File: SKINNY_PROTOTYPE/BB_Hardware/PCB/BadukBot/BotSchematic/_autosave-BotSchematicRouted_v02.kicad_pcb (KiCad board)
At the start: 4 copper layers, 93 x 44.5 mm, 82 parts, among them J1 MOLEX_78171-0002, J10 A3-16DA-2SV(71), J11 62401621722, J12 A3-16DA-2SV(71), J13 0877601616, J2 MOLEX_78171-0003, M1 Pos-1a, M2 Neg-1a, M3 Pos-2a, M4 Neg-2a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

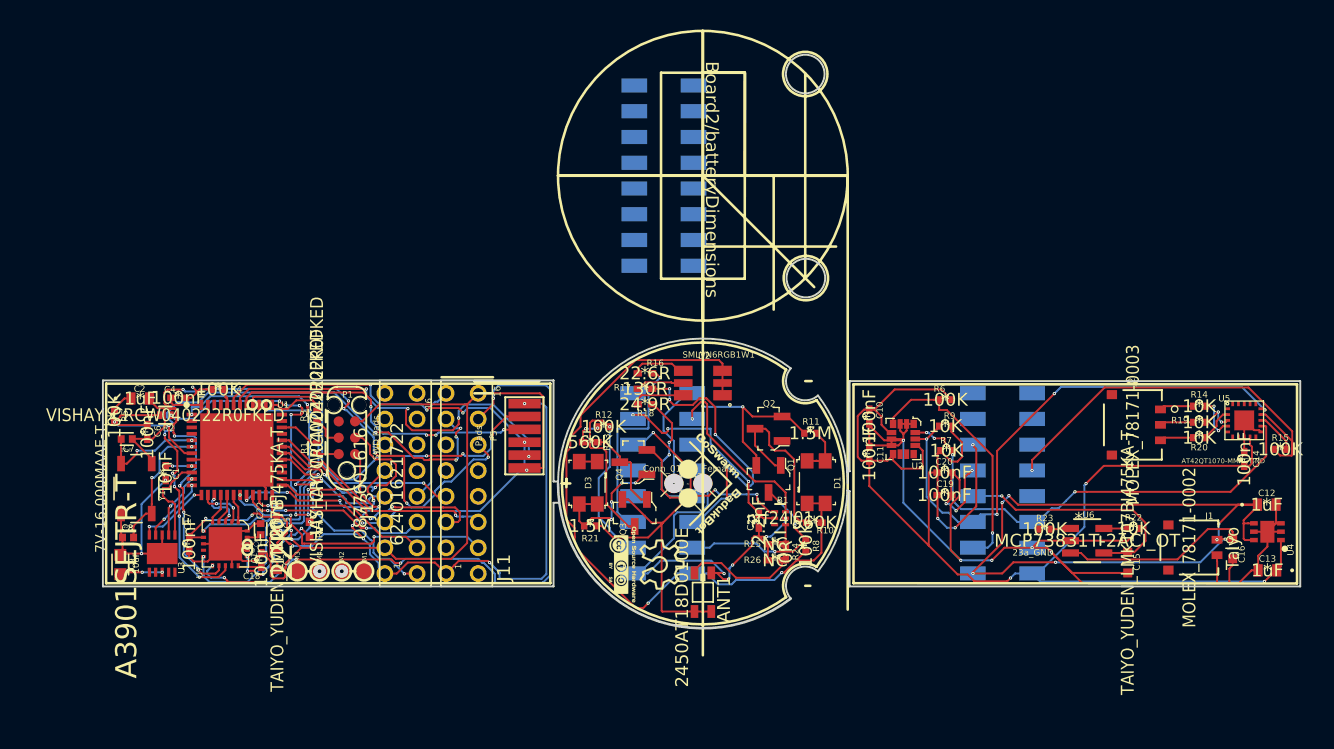
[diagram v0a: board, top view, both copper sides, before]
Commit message: Routed PCBs pending optimization
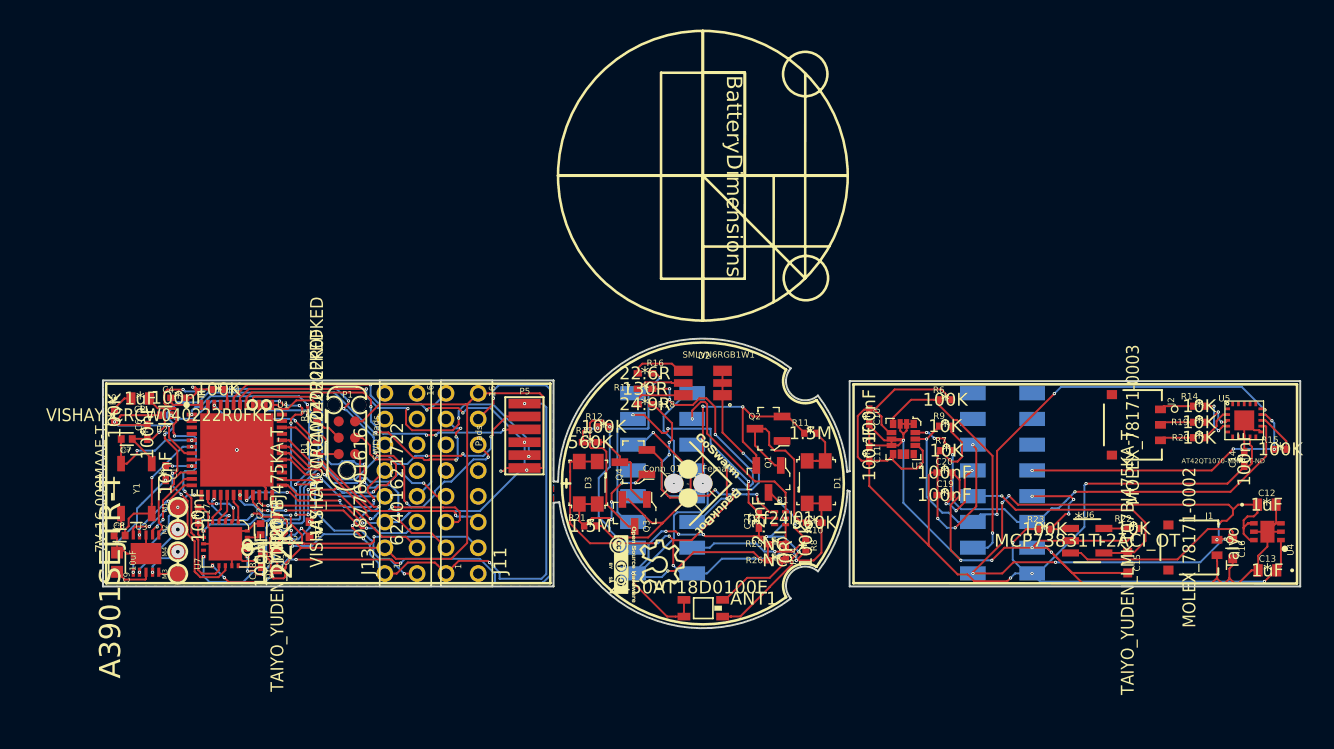
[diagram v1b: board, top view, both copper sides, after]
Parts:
- removed the J12 at (113.9, 83.9)
- J10, J12: footprint A13:A13 -> A13:A13_1
- moved M1 15.3 mm to (75.5, 109.6), turned to 180 degrees
- moved M2 13.1 mm to (75.5, 111.3), turned to 180 degrees
- moved M4 11.1 mm to (75.5, 113.1), turned to 180 degrees
- moved M3 9.29 mm to (75.5, 114.8), turned to 180 degrees
- moved C17 2.32 mm to (77.1, 110.2), turned to 270 degrees
- moved U3 1.25 mm to (73.0, 113.2)
- moved ANT1 1.24 mm to (116.3, 117.5), turned to 180 degrees
- moved C8 0.67 mm to (71.0, 111.8)
- moved C9 0.31 mm to (70.8, 113.9)
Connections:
- J12 pad 10: 23a_Ground -> Net-(J12-Pad10)
- J12 pad 12: 21a_3.3v -> Net-(J12-Pad12)
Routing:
- net 2a_GND: track 12.4 -> 98.3 mm, vias 5 -> 12
- net 15a_GND2: track 69.6 -> 0.00 mm, vias 4 -> 0
- net 3b_PHOTODIODE1: track 0.00 -> 26.6 mm, vias 0 -> 6
- net ~29a_TOUCH_CHG~: track 32.6 -> 22.9 mm, vias 1 -> 4
- net 27a_CHARGING: track 1.56 -> 8.08 mm, vias 0 -> 3
- net Net-(M1-Pad1): track 0.00 -> 6.48 mm, vias 0 -> 2
- net 21a_3.3v: track 115.9 -> 121.3 mm, vias 6 -> 8
- net Net-(M2-Pad1): track 0.00 -> 4.55 mm, vias 1 -> 2
- net 2b_GND: track 115.1 -> 118.8 mm, vias 9 -> 13
- net Net-(M4-Pad1): track 0.00 -> 2.89 mm, vias 1 -> 2
- net Net-(ANT1-Pad1): track 8.85 -> 6.47 mm
- net 10b_SDA: track 51.9 -> 53.7 mm
- net Net-(M3-Pad1): track 0.00 -> 1.53 mm
- net 1a_3.3v: track 59.9 -> 58.4 mm, vias 4 -> 8
- net 1b_3.3v: track 75.7 -> 74.4 mm, vias 13 -> 11
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- added copper zone on F.Cu, net 1b_3.3v
- added copper zone on B.Cu, net 2b_GND
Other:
- board size 93 x 44.5 mm -> 93 x 22.5 mm
- copper layers 4 -> 2
- board text added: "BatteryDimensions"
- board text added: "j13-10"
- board text added: "j13-12"
- board text removed: "10"
- board text removed: "12"
- board text removed: "23a_GND"
- board text removed: "Board2/batteryDimensions"

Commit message: Updates to the BOM; PCB changes
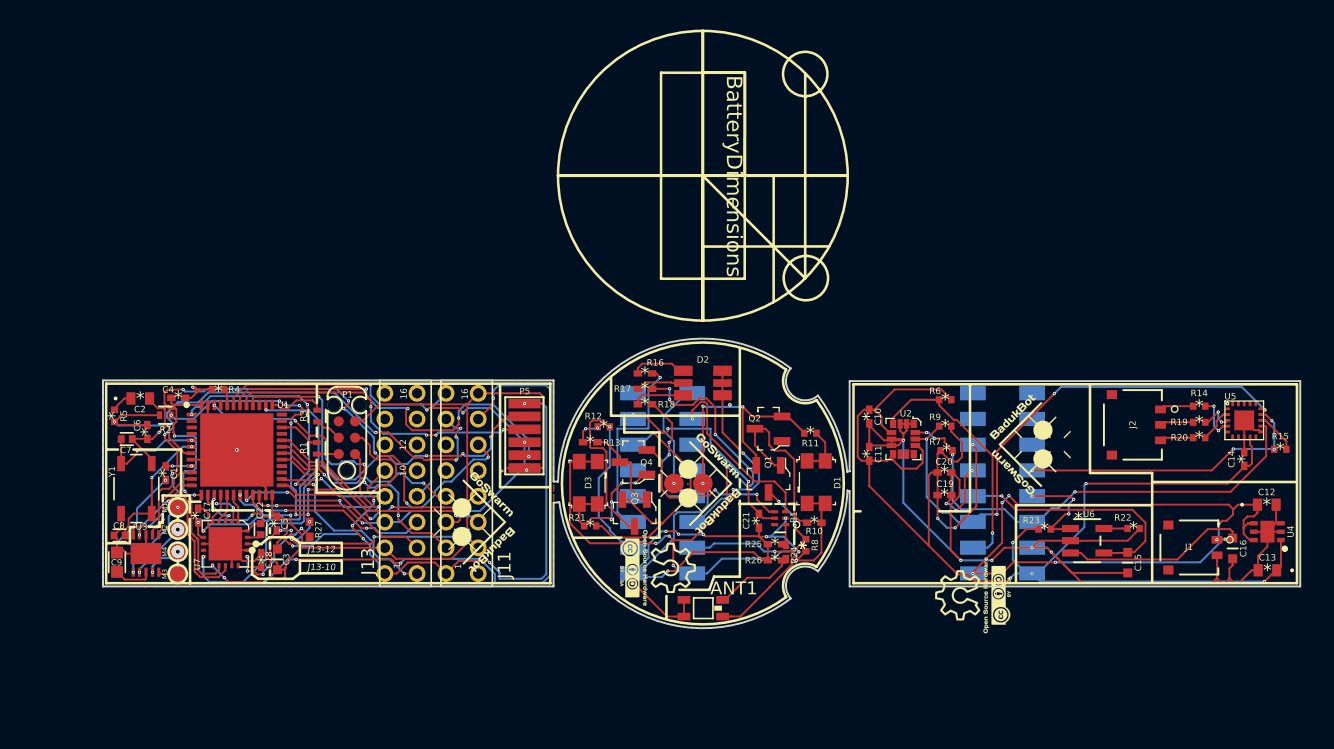
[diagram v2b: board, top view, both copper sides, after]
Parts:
- added G1: LOGO, Silk:BadukBot-GoSwarm, F.Cu at (141.8, 104.8)
- added G1: LOGO, Silk:BadukBot-GoSwarm, F.Cu at (98.5, 110.8)
- added G2: LOGO, Silk:OpenHardwareLogo, F.Cu at (137.2, 116.5)
- added G2: LOGO, Silk:OpenHardwareLogo, B.Cu at (94.2, 107.8)
- moved G2 0.91 mm to (112.8, 114.3)
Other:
- board text added: "10"
- board text added: "12"
- board text added: "J13-10"
- board text added: "J13-12"
- board text removed: "j13-10"
- board text removed: "j13-12"

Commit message: Updated copper cores; changed schematic naming flags for 3rd party BOM generator; added renders of board; added some datasheets
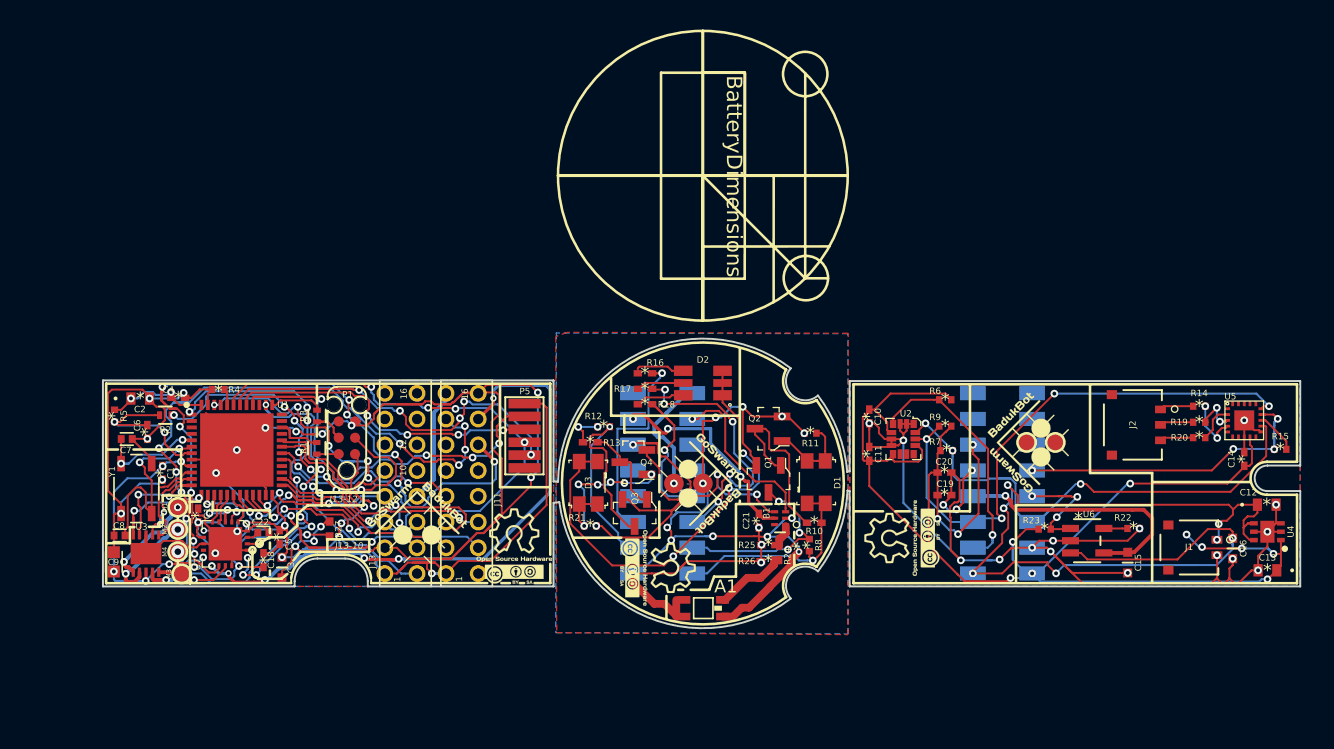
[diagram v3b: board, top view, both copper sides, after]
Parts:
- removed ANT1: 2450AT18D0100E, 2450AT18D0100E:DFN320X160X120-4RN
- added A1: 2450AT18D0100E, 2450AT18D0100E:DFN320X160X120-4RN, F.Cu at (116.3, 117.5)
- added G5: LOGO, Silk:links_20mm, B.Cu at (80.2, 108.2)
- added G6: LOGO, Silk:links_20mm, B.Cu at (152.7, 109.3)
- added G7: LOGO, Silk:links_20mm, B.Cu at (119.6, 107.7)
- added TESTPOINT-50MIL: VAL**, gsg-modules:TESTPOINT-50MIL, F.Cu at (143.7, 104.6)
- added TESTPOINT-50MIL: VAL**, gsg-modules:TESTPOINT-50MIL, F.Cu at (141.4, 104.6)
- C19: value 100nF -> 10nF
- C20: value 100nF -> 1nF
- G2: moved to F.Cu
- J1: value MOLEX_78171-0002 -> MOLEX781710002
- J10, J12: value A3-16DA-2SV(71) -> A316DA2SV71
- J2: value MOLEX_78171-0003 -> MOLEX781710003
- M1: value Pos-1a -> Pos1a
- M2: value Neg-1a -> Neg1a
- M3: value Pos-2a -> Pos2a
- M4: value Neg-2a -> Neg2a
- P1: value SWD Pads -> SWDPads
- P4: value Conn_01x02_Female -> Conn01x02Female
- U3: value A3901SEJTR-T -> A3901SEJTRT
- U4: value ADP122ACPZ-3.3-R7 -> ADP122ACPZ33R7
- U5: value AT42QT1070-MMHCT-ND -> AT42QT1070MMHCTND
- U6: value MCP73831T-2ACI_OT -> MCP73831T2ACIOT
- U7: value NRF24L01P-R7 -> NRF24L01PR7
- Y1: value 7V-16.000MAAE-T -> 7V16000MAAET
- moved G2 8.86 mm to (101.6, 112.6), turned to 0 degrees
- moved G2 7.07 mm to (131.8, 112.0)
- moved G1 4.38 mm to (94.1, 110.9), turned to 315 degrees
- moved R27 1.55 mm to (87.3, 111.3)
- moved C5 1.07 mm to (83.4, 111.9)
- moved C3 0.73 mm to (83.6, 114.3)
- moved R24 0.52 mm to (122.2, 113.1)
- moved R25 0.52 mm to (121.4, 112.5)
- moved R26 0.52 mm to (121.4, 113.8)
- moved C22 0.34 mm to (82.1, 111.6), turned to 0 degrees
- moved M3 0.31 mm to (75.8, 114.8)
- moved R8 0.27 mm to (124.5, 112.5)
- moved C1 0.26 mm to (74.3, 106.9)
- moved C9 0.25 mm to (70.5, 113.8)
- moved G1 0.21 mm to (141.7, 104.6)
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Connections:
- net 10b_SDA renamed 10bSDA
- net 11b_SCL renamed 11bSCL
- net 12a_ANT1 renamed 12aA1
- net 12b_ANT1 renamed 12bA1
- net 13a_ANT2 renamed 13aA2
- net 13b_ANT2 renamed 13bA2
- net 14a_VDD_PA renamed 14aVDDPA
- net 14b_VDD_PA renamed 14bVDDPA
- net 15a_P4-1 renamed 15aP41
- net 15b_P4-1 renamed 15bP41
- net 1a_3.3v renamed 1a33v
- net 1b_3.3v renamed 1b33v
- net 22a_VBAT renamed 22aVBAT
- net 22b_VBAT renamed 22bVBAT
- net 24a_IMU_INT renamed 24aIMUINT
- net 24b_IMU_INT renamed 24bIMUINT
- net 25a_SDA renamed 25aSDA
- net 26a_SCL renamed 26aSCL
- net 27a_CHARGING renamed 27aCHARGING
- net 27b_CHARGING renamed 27bCHARGING
- net 28a_P4-1 renamed 28aP41
- net 2a_GND renamed 2aGND
- net 2b_GND renamed 2bGND
- net 3a_PHOTODIODE1 renamed 3aPHOTODIODE1
- net 3b_PHOTODIODE1 renamed 3bPHOTODIODE1
- net 4a_PHOTODIODE2 renamed 4aPHOTODIODE2
- net 4b_PHOTODIODE2 renamed 4bPHOTODIODE2
- net 5a_RGBLED1 renamed 5aRGBLED1
- net 5b_RGBLED1 renamed 5bRGBLED1
- net 6a_RGBLED2 renamed 6aRGBLED2
- net 6b_RGBLED2 renamed 6bRGBLED2
- net 7a_RGBLED3 renamed 7aRGBLED3
- net 7b_RGBLED3 renamed 7bRGBLED3
- net 8b_IO1 renamed 8bIO1
- net 9b_IO2 renamed 9bIO2
- net MCU_X1_16MHZ renamed MCUX116MHZ
- net MCU_X2_16MHZ renamed MCUX216MHZ
- net MOTOR_CONTROL1 renamed MOTORCONTROL1
- net MOTOR_CONTROL2 renamed MOTORCONTROL2
- net MOTOR_CONTROL3 renamed MOTORCONTROL3
- net MOTOR_CONTROL4 renamed MOTORCONTROL4
- net RADIO_IRQ renamed RADIOIRQ
- net ~29a_TOUCH_CHG~ renamed ~29aTOUCHCHG~
- net ~29b_TOUCH_CHG~ renamed ~29bTOUCHCHG~
- C10 pad 1: 21a_3.3v -> 21a33v
- C10 pad 2: 23a_Ground -> 23aGround
- C11 pad 1: 21a_3.3v -> 21a33v
- C11 pad 2: 23a_Ground -> 23aGround
- C12 pad 2: 23a_Ground -> 23aGround
- C13 pad 1: 21a_3.3v -> 21a33v
- C13 pad 2: 23a_Ground -> 23aGround
- C14 pad 1: 21a_3.3v -> 21a33v
- C14 pad 2: 23a_Ground -> 23aGround
- C15 pad 2: 23a_Ground -> 23aGround
- C16 pad 2: 23a_Ground -> 23aGround
- C19 pad 1: 23a_Ground -> 23aGround
- C19 pad 2: 21a_3.3v -> 21a33v
- C20 pad 2: 21a_3.3v -> 21a33v
- J1 pad 2: 23a_Ground -> 23aGround
- J12 pad 1: 21a_3.3v -> 21a33v
- J12 pad 3: 23a_Ground -> 23aGround
- R15 pad 2: 21a_3.3v -> 21a33v
- R22 pad 1: 23a_Ground -> 23aGround
- R23 pad 1: 21a_3.3v -> 21a33v
- R6 pad 2: 21a_3.3v -> 21a33v
- R7 pad 2: 21a_3.3v -> 21a3.3v
- R9 pad 2: 21a_3.3v -> 21a3.3v
- U1 pad 29: RADIO_CLK -> RADIOCLK
- U2 pad 1: 23a_Ground -> 23aGround
- U2 pad 12: 21a_3.3v -> 21a33v
- U2 pad 2: 23a_Ground -> 23aGround
- U2 pad 3: 23a_Ground -> 23aGround
- U2 pad 5: 21a_3.3v -> 21a33v
- U2 pad 6: 23a_Ground -> 23aGround
- U2 pad 7: 23a_Ground -> 23aGround
- U2 pad 8: 21a_3.3v -> 21a33v
- U4 pad 1: 21a_3.3v -> 21a33v
- U4 pad 2: 23a_Ground -> 23aGround
- U4 pad 3: 23a_Ground -> 23aGround
- U4 pad 5: 23a_Ground -> 23aGround
- U4 pad 7: 23a_Ground -> 23aGround
- U5 pad 11: 23a_Ground -> 23aGround
- U5 pad 13: 23a_Ground -> 23aGround
- U5 pad 44: 23a_Ground -> 23aGround
- U5 pad 8: 23a_Ground -> 23aGround
- U5 pad 9: 23a_Ground -> 23aGround
- U6 pad 2: 23a_Ground -> 23aGround
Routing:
- net 2aGND: track 98.4 -> 0.00 mm, vias 12 -> 17
- net 2a_GND: track 0.00 -> 97.5 mm
- net 2bGND: track 118.8 -> 167.9 mm, vias 13 -> 19
- net 1b33v: track 74.4 -> 121.6 mm, vias 11 -> 18
- net 22aVBAT: track 72.4 -> 86.0 mm
- net 7a_RGBLED3: track 0.00 -> 12.4 mm, vias 0 -> 1
- net 7aRGBLED3: track 9.94 -> 0.00 mm, vias 2 -> 0
- net Net-(J12-Pad12): track 0.00 -> 9.86 mm, vias 0 -> 2
- net 12bA1: track 55.7 -> 64.9 mm, vias 8 -> 10
- net ~29bTOUCHCHG~: track 14.6 -> 23.1 mm
- net 23a_Ground: track 98.4 -> 91.6 mm, vias 8 -> 0
- net 8bIO1: track 30.7 -> 37.3 mm
- net Net-(P1-Pad3): track 36.1 -> 29.6 mm, vias 10 -> 8
- net MCUX216MHZ: track 10.3 -> 15.8 mm
- net 13bA2: track 48.1 -> 53.4 mm, vias 7 -> 9
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- added copper zone on B.Cu, net 1a33v
- added copper zone on B.Cu, net 1b33v
- added copper zone on F.Cu, net 21a33v
- added copper zone on B.Cu, net 23a_Ground
- added copper zone on F.Cu, net 2aGND
- added copper zone on F.Cu, net 2bGND
- removed copper zone on F.Cu, net 1b33v
- removed copper zone on B.Cu, net 2bGND
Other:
- outline, holes or cut-outs redrawn
- net class Default: via_dia 0.254 -> 0.6; via_drill 0.1016 -> 0.3
